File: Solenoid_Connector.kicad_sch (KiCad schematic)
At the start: 10 parts, among them J13 DSUB_15pin/VGA Veritical Fema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, J14 Conn_01x03_Pin, J15 DSUB_15pin/VGA Veritical Fema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, J16 Conn_01x03_Pin, J17 DSUB_15pin/VGA Veritical Fema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, J18 Conn_01x03_Pin, J19 DSUB_15pin/VGA Veritical Fema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, J20 Conn_01x03_Pin, J21 DSUB_15pin/VGA Veritical Fema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, J9 Conn_01x03_Pin

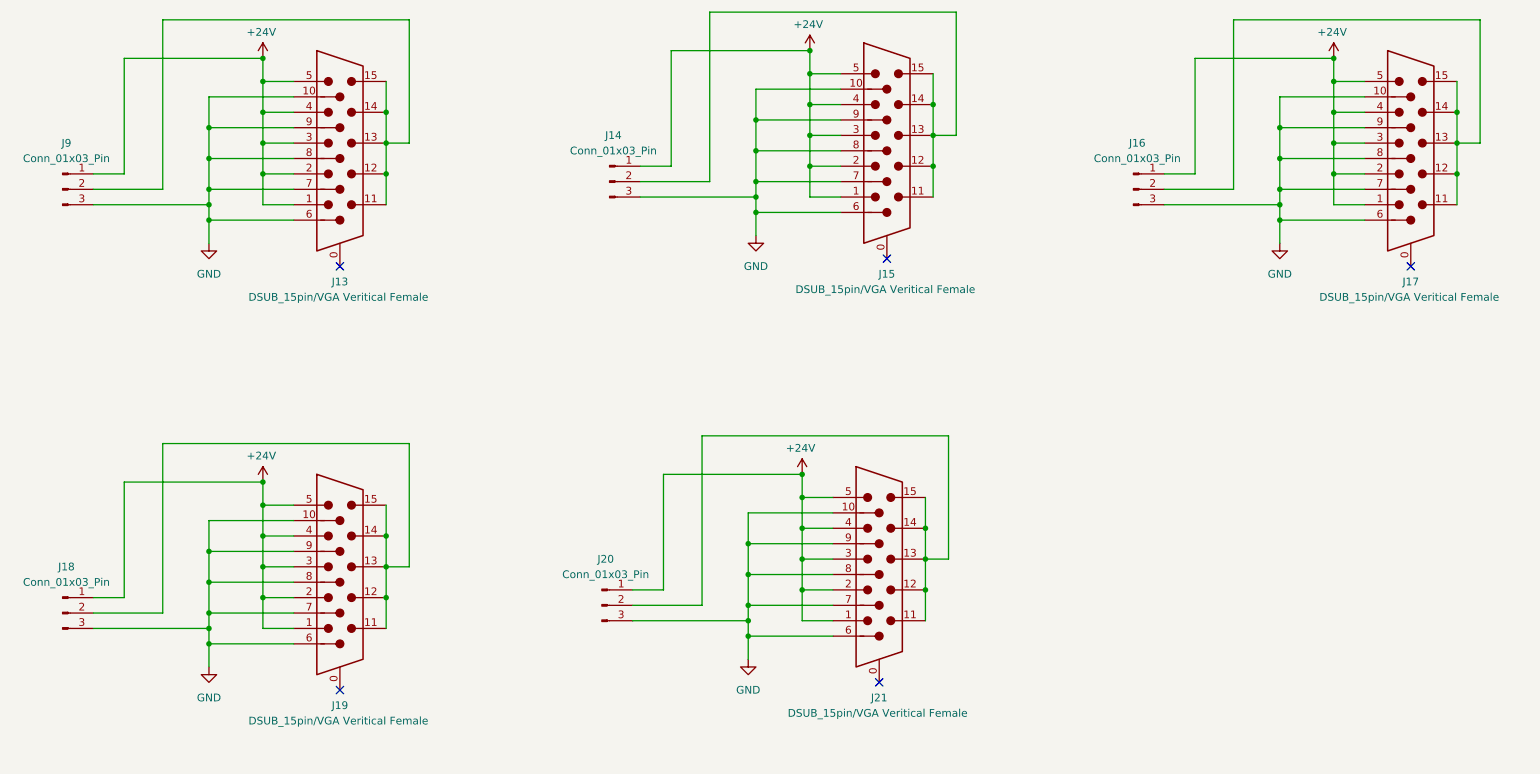
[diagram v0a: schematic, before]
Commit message: silkscreen labeling, fixed trace thicknesses
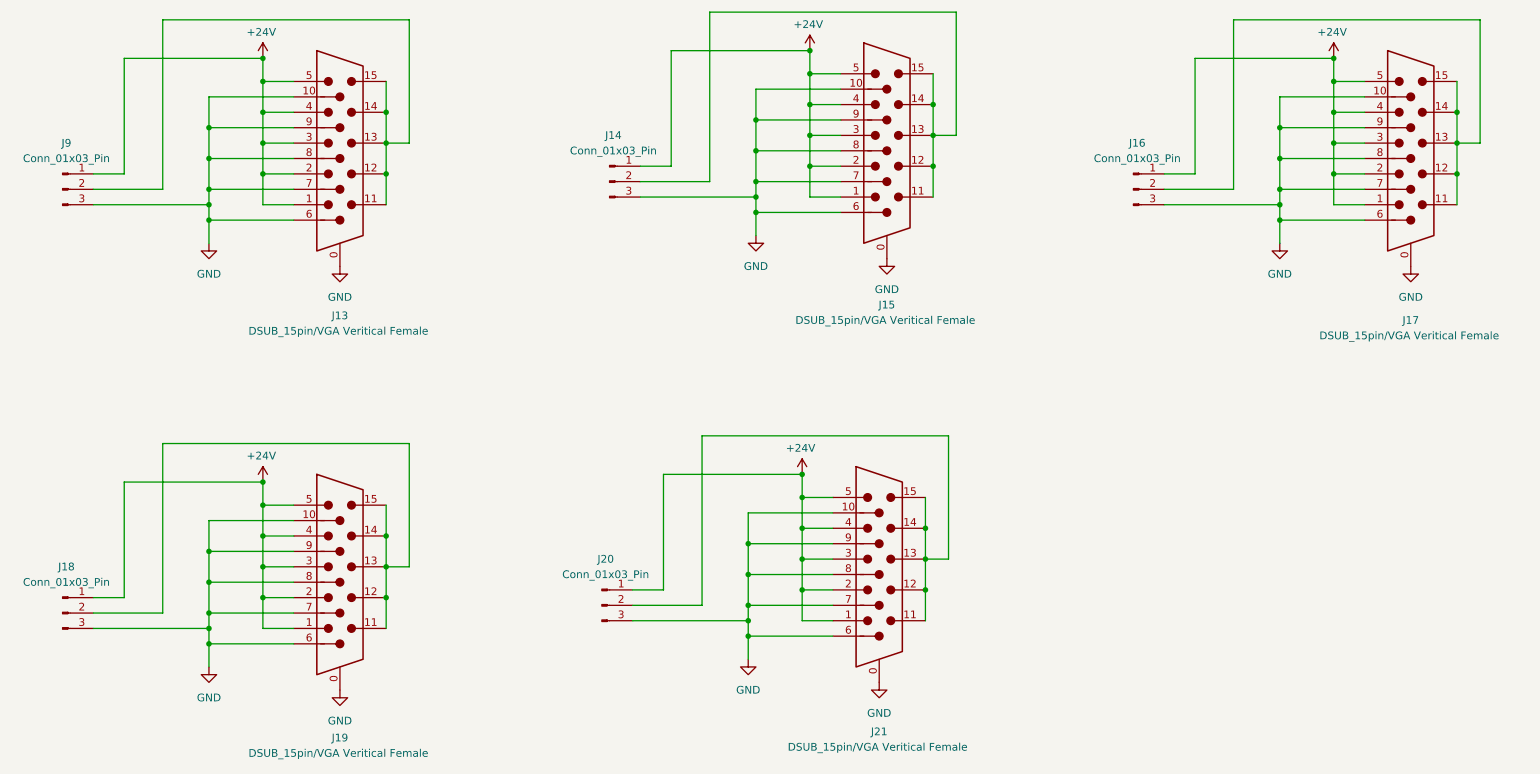
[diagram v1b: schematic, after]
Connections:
- net GND: now also J13.0, J15.0, J17.0, J19.0, J21.0
- no-connect marks 5 -> 0
